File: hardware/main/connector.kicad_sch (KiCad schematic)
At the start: 22 parts, among them J11 TF-01A, J3 Conn_01x04, J4 Conn_01x04, J5 Conn_01x04, J6 Conn_01x04, J7 Conn_01x10, J7b Conn_01x08, J8 Conn_01x06, J9 Conn_01x04

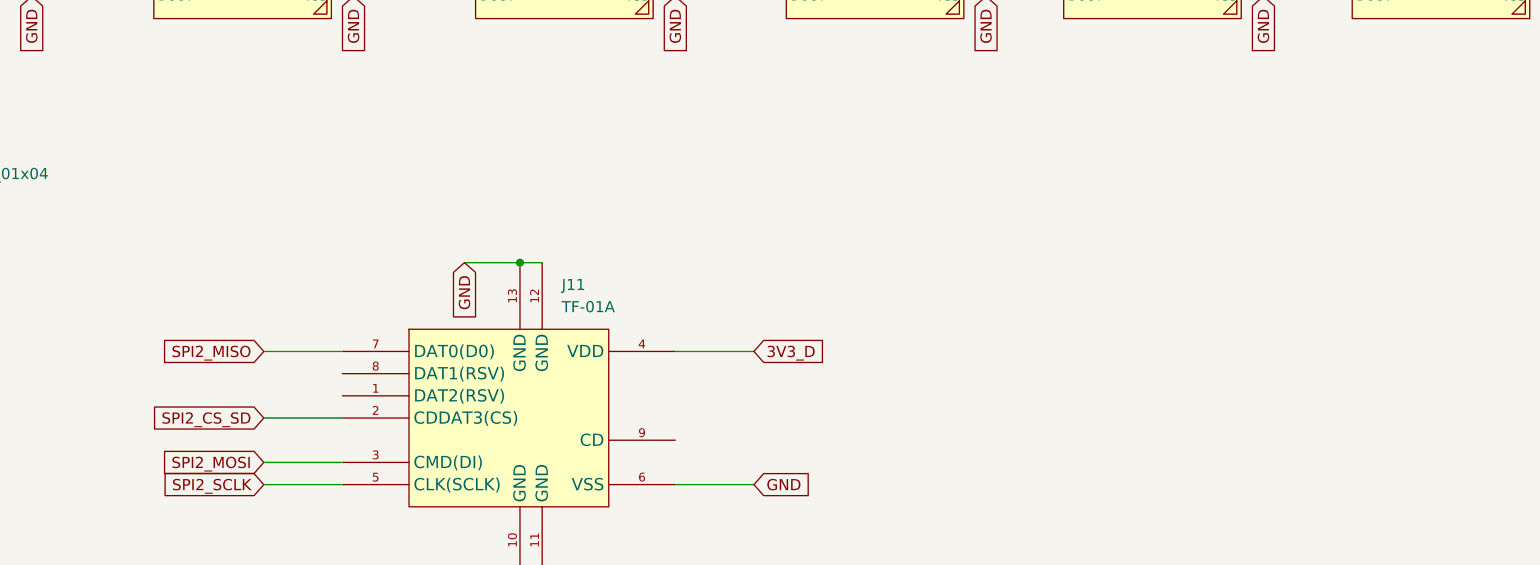
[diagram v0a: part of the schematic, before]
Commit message: hardware: pull-ups carte SD, resistances serie d'horloge, timer de charge
Trois points "important" de l'audit 2026-09-23, verifies un par un sur le
schema avant modification (tools/kicad_netlist.py).

H7 — carte SD : aucune pull-up sur J11. L'ESP-IDF les rend obligatoires
(sd_pullup_requirements.rst : « en mode SPI ou SD 1 bit, CMD et DAT0-DAT3
doivent etre tirees au plus par 10k, y compris les lignes non reliees a
l'hote »). Ajout de R15-R19 (10k) sur un rail 3V3_D commun, feuille connector.
DAT1 (J11.8) et DAT2 (J11.1) n'avaient aucun fil : nets nommes SD_DAT1/SD_DAT2.

H8 — horloges SPI : FB1/FB2 (ferrites 120R) remplacees par R13/R14 = 22 ohm
0603. Device:R et Device:FerriteBead ont leurs pins au meme endroit, donc les
fils et la connectivite sont inchanges. Une ferrite sur une horloge rapide
arrondit les fronts et viole les timings de la carte (ESP-IDF sdspi_share.rst,
AC loading) ; les yeux tournent a 40 MHz, 80 visees. Ajout de C6/C7, 10 pF vers
GND en DNP, comme provision jusqu'au test CEM.

H9 — charge LiPo : TMR etait cable directement a GND, c'est-a-dire timers de
securite desactives (bq24075 §6.1). Ajout de R_TMR 56k 1 % entre TMR et GND
-> t_MAXCHG = 10 x K_TMR x R_TMR = 5,6 a 9,3 h (K_TMR 36-60 s/kOhm), pour une
charge de ~4 h a 1 A sur 3000 mAh. Plage admissible datasheet : 18-72 kOhm.

A4 — ICS-43434 sans decouplage : CONSTAT ERRONE, aucune modification faite.
C3 (100 nF 0402, 3V3_A/GND) est deja place a cote de U4 et l'etait deja dans le
fichier du 23/09. Seule subsiste une contrainte de layout (au plus pres des
broches 5 et 3, sans via). Le rapport d'audit et la fiche datasheet sont annotes
en consequence.

tools/kicad_edit.py : helpers d'edition de schema (symboles, fils, labels,
jonctions, remplacement de composant a geometrie de pins identique).
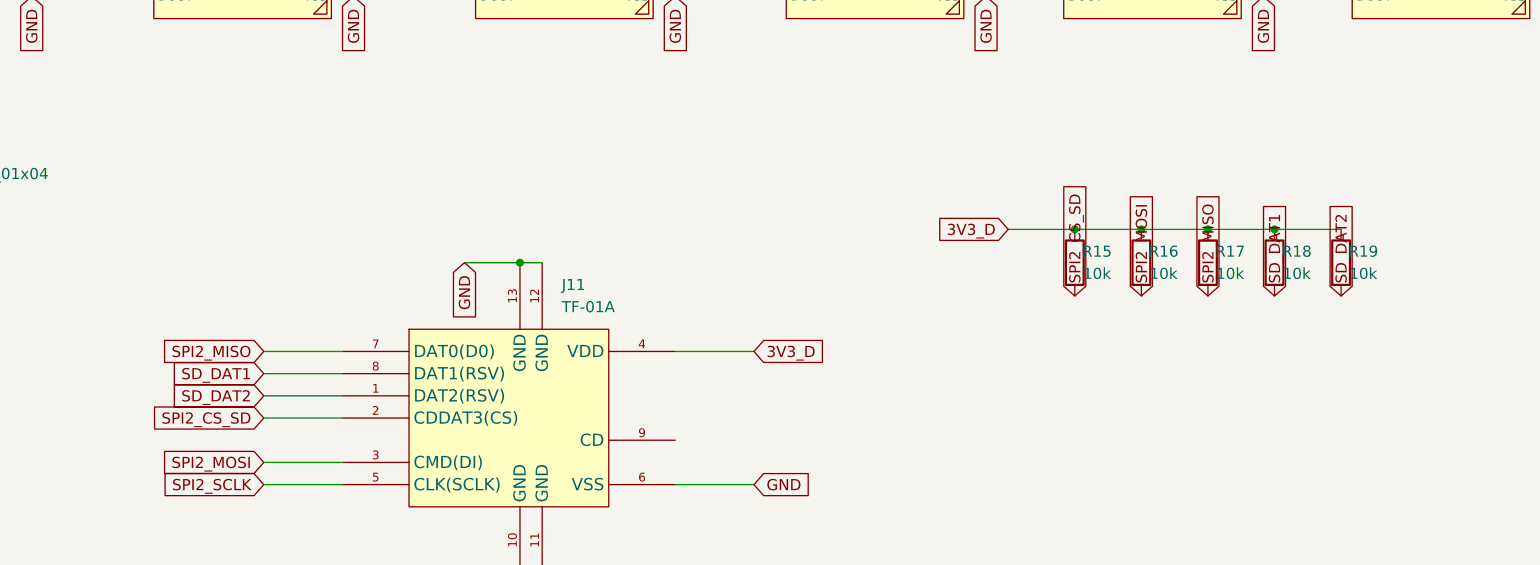
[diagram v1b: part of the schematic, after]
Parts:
- added R15, R16, R17, R18, R19: 10k, Resistor_SMD:R_0402_1005Metric, symbol Device:R
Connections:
- net 3V3_D: now also R15.1, R16.1, R17.1, R18.1, R19.1
- net SPI2_CS_SD: now also R15.2
- net SPI2_MISO: now also R17.2
- net SPI2_MOSI: now also R16.2
- net SD_DAT2: now reaches J11.1 (DAT2(RSV))
- net SD_DAT2: now also R19.2
- net SD_DAT1: now reaches J11.8 (DAT1(RSV))
- net SD_DAT1: now also R18.2

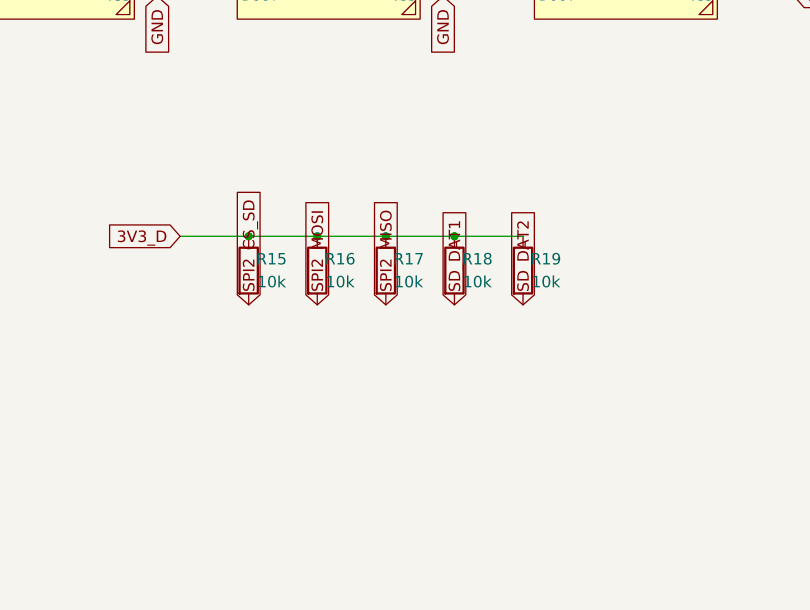
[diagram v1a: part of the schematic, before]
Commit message: hardware(power): U5 (3V3_D) en SO-8 — AP2112M-3.3TRG1
Audit 2026-09-23 H5 : en SOT-25 (theta JA 184 C/W), U5 dissipe 0,56 W sous USB
a 400 mA, soit +103 C d'elevation en boitier ferme. Le SO-8 (114 C/W) ramene
l'elevation a +64 C — meilleur que le SOT-89-5 envisage dans l'audit (120 C/W),
et surtout disponible chez LCSC (C5290219), ce que n'etait pas le SOT-89-5.

U6 (3V3_A) reste en SOT-25 : il n'alimente que le PCM5122, ~25 mA, il ne
chauffe pas. Deux references du meme LDO dans la BOM, assume.

Brochage SO-8 releve sur le dessin de la datasheet (le tableau correspondant
n'est pas extractible en texte, et les sources web se contredisaient) :
1 = VOUT, 2/3/4 = NC, 5 = EN, 6+7 = GND, 8 = VIN. Il n'a rien de commun avec
celui du SOT-25 (1 = VIN, 2 = GND, 3 = EN, 5 = VOUT).

Symbole : la bibliotheque KiCad officielle ne contient que les variantes K
(SOT-25), le symbole a donc ete cree dans la bibliotheque projet
`lcsc_imported`, avec les positions de broches du symbole officiel — VIN, EN et
VOUT retombent ainsi exactement sur les fils deja en place. Seules les deux
masses (6 et 7) ont demande un fil, et le global label GND existant se trouvait
deja pile entre elles.

Verifie par netlist : VIN->VSYS, EN->EN_SYS, VOUT->3V3_D, GND sur les deux
broches, 3V3_D intact avec ses 28 consommateurs, U6 inchange.

Reste a faire au layout : plan de cuivre genereux sous et autour de U5.
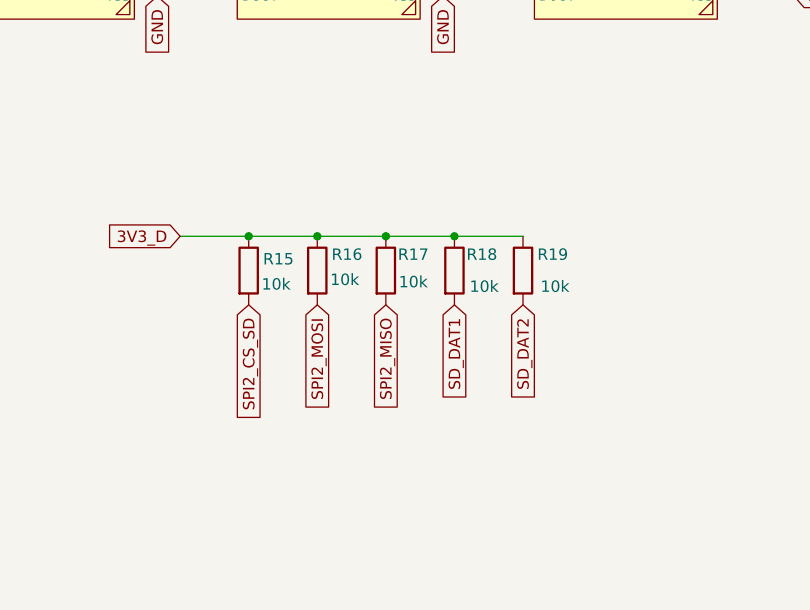
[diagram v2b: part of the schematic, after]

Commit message: hardware(power): corrections issues de l'ERC — jonction L1 et empreintes JST
Deux points remontes par l'ERC du 2026-09-27 (0 erreur, 148 warnings).

1. REGRESSION de ma part, corrigee : en isolant l'EN de U7 pour le net EN_SYS,
   j'avais aussi supprime la jonction (105.41, 111.76) en la croyant devenue
   inutile. Elle portait en realite une seconde derivation : VSYS -> L1,
   l'inductance du boost. Sans elle, KiCad signalait une extremite de fil non
   connectee — autrement dit le MT3608 n'etait plus alimente. Jonction
   retablie, L1.1 de nouveau sur VSYS (verifie par netlist).
   Lecon : une jonction peut porter plus de branches que celle qu'on retire ;
   verifier ce qui passe par le point avant de la supprimer.

2. Empreintes JST PH introuvables (J2, J9, J10) : le projet utilisait
   « ...1x02-P2.00mm... » alors que la bibliotheque KiCad nomme
   « ...1x02_P2.00mm... » (underscore et non tiret). Defaut preexistant sur J2
   et J9, que j'avais propage a J10 en copiant J9. Les trois noms sont
   corriges et verifies contre la bibliotheque officielle, de meme que toutes
   les empreintes ajoutees depuis (SOIC-8, SOT-23, L_0805, R_0603, R_0402,
   C_0402, JST_SH 1x02).
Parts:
- J9: footprint Connector_JST:JST_PH_B4B-PH-K_1x04-P2.00mm_Vertical -> Connector_JST:JST_PH_B4B-PH-K_1x04_P2.00mm_Vertical
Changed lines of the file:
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@@
 			)
 		)
-		(property "Footprint" "Connector_JST:JST_PH_B4B-PH-K_1x04-P2.00mm_Vertical"
+		(property "Footprint" "Connector_JST:JST_PH_B4B-PH-K_1x04_P2.00mm_Vertical"
 			(at 49.53 127 0)
 			(hide yes)
